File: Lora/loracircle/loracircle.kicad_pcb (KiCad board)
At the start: 2 copper layers, 8 parts, among them J1 CONMHF1-SMD-T, U1 RFM69HCW

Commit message: lora done i think
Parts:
- added REF**: 20x20pads, Library:20x20pads, F.Cu at (139.7, 130.8)
- JP3: moved to B.Cu
- moved JP3 45.0 mm to (139.7, 130.8)
- moved R2 33.2 mm to (130.2, 138.8), turned to -135 degrees
- moved R3 32.0 mm to (131.7, 140.2), turned to -135 degrees
- moved C1 23.7 mm to (144.7, 120.9), turned to 135 degrees
- moved J1 22.6 mm to (148.7, 123.4), turned to -135 degrees
- moved C2 17.8 mm to (145.3, 139.7)
- moved C3 17.8 mm to (145.3, 141.6)
- moved U1 4.18 mm to (139.7, 130.8)
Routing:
- net 3.3V: track 0.00 -> 60.9 mm, vias 0 -> 3
- net /RST_3V: track 0.00 -> 24.2 mm, vias 0 -> 1
- net /CS_3V: track 0.00 -> 22.5 mm, vias 0 -> 1
- net /MISO_3V: track 0.00 -> 17.7 mm, vias 0 -> 1
- net /MOSI_3V: track 0.00 -> 16.2 mm, vias 0 -> 1
- net /DIO0: track 0.00 -> 12.0 mm, vias 0 -> 1
- net /SCK_3V: track 0.00 -> 11.4 mm, vias 0 -> 1
- net Net-(U1-ANT): track 0.00 -> 6.38 mm
- net GND: track 0.00 -> 5.52 mm, vias 0 -> 72
- added copper zone on F.Cu, net GND
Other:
- board outline added: 25 x 25 mm
- board text added: "lora"
- board text added: "projectrocketship"
- board text added: "rev1-@sjacksonhodum"
- board text added: "revision 1"

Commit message: prettify lora board
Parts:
- C1, C3: footprint LIBRARY:0805-NO -> Capacitor_SMD:C_0805_2012Metric
- C2: footprint LIBRARY:0805-NO -> Capacitor_SMD:C_0603_1608Metric
- JP3: footprint LIBRARY:CONN_B9B-PH-SM4-TB_JST -> Connector_JST:JST_PH_B9B-PH-SM4-TB_1x09-1MP_P2.00mm_Vertical
- R2, R3: footprint LIBRARY:0805-NO -> Resistor_SMD:R_0603_1608Metric
- moved JP3 1.07 mm to (139.6, 129.8)
- moved C2 0.80 mm to (145.2, 138.9), turned to 45 degrees
- moved C3 0.72 mm to (145.8, 141.0), turned to -135 degrees
- moved R2 0.37 mm to (130.0, 138.5)
- moved R3 0.37 mm to (131.4, 139.9)
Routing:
- net GND: track 5.52 -> 36.9 mm, vias 72 -> 5
- net 3.3V: track 60.9 -> 53.3 mm, vias 3 -> 2
- net /SCK_3V: track 11.4 -> 13.8 mm, vias 1 -> 2
- net /MISO_3V: track 17.7 -> 19.6 mm
- net /CS_3V: track 22.5 -> 20.9 mm
- net /DIO0: track 12.0 -> 11.4 mm
- net /RST_3V: track 24.2 -> 23.6 mm
- added copper zone on B.Cu, net GND
- removed copper zone on F.Cu, net GND
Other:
- board text added: "@iceches"
- board text added: "@sjacksonhodum"
- board text removed: "lora"
- board text removed: "projectrocketship"
- board text removed: "rev1-@sjacksonhodum"
- board text removed: "revision 1"

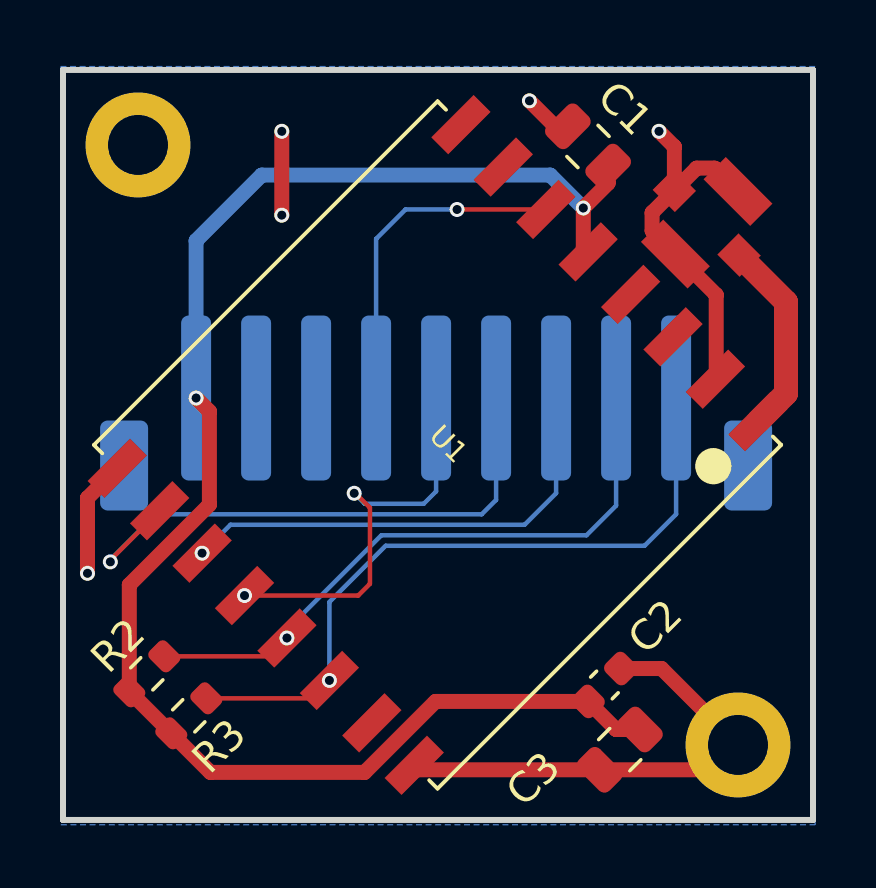
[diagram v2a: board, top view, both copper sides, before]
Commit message: Update lora silkscreen
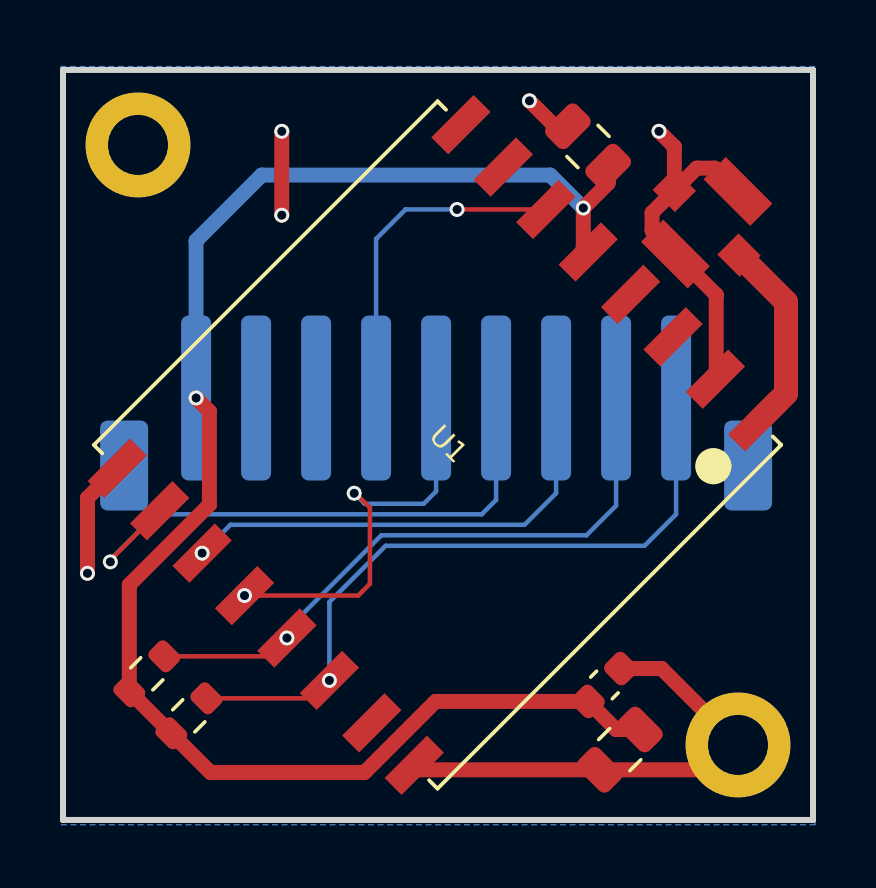
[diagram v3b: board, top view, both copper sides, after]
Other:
- board text added: "lora module -- revision 1"
- board text added: "projectrocketship"
